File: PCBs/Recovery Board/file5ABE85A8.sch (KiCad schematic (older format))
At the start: 3 parts

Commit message: review changes + instr board PCB
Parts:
- gave numbers to parts that had none: 3
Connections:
- net VccA: now also U2.5 (EN)
- net VccB: no longer U2.5 (EN)
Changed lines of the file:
@@
 $EndDescr
 $Comp
-L PI4ULS5V201TAEX U?
+L PI4ULS5V201TAEX U2
 U 1 1 5ABE85EB
 P 5400 3750
-F 0 "U?" H 5400 4300 60  0000 C CNN
+AR Path="/5ABE85A9/5ABE85EB" Ref="U2"  Part="1"
+AR Path="/5ABEAE41/5ABE85EB" Ref="U3"  Part="1"
+F 0 "U3" H 5400 4300 60  0000 C CNN
 F 1 "PI4ULS5V201TAEX" H 5400 3650 60  0000 C CNN
 F 2 "" H 5400 3750 60  0001 C CNN
@@
 $EndComp
 $Comp
-L C C?
+L C C6
 U 1 1 5ABE8664
 P 6250 3950
-F 0 "C?" H 6275 4050 50  0000 L CNN
+AR Path="/5ABE85A9/5ABE8664" Ref="C6"  Part="1"
+AR Path="/5ABEAE41/5ABE8664" Ref="C8"  Part="1"
+F 0 "C8" H 6275 4050 50  0000 L CNN
 F 1 "0.1uF" H 6275 3850 50  0000 L CNN
 F 2 "" H 6288 3800 50  0001 C CNN
@@
 $EndComp
 $Comp
-L C C?
+L C C5
 U 1 1 5ABE8691
 P 4550 3800
-F 0 "C?" H 4575 3900 50  0000 L CNN
+AR Path="/5ABE85A9/5ABE8691" Ref="C5"  Part="1"
+AR Path="/5ABEAE41/5ABE8691" Ref="C7"  Part="1"
+F 0 "C7" H 4575 3900 50  0000 L CNN
 F 1 "0.1uF" H 4575 3700 50  0000 L CNN
 F 2 "" H 4588 3650 50  0001 C CNN
@@
 	4550 3400 4950 3400
 $Comp
-L GND #PWR?
+L GND #PWR16
 U 1 1 5ABE86F6
 P 4550 3950
-F 0 "#PWR?" H 4550 3700 50  0001 C CNN
+AR Path="/5ABE85A9/5ABE86F6" Ref="#PWR16"  Part="1"
+AR Path="/5ABEAE41/5ABE86F6" Ref="#PWR19"  Part="1"
+F 0 "#PWR19" H 4550 3700 50  0001 C CNN
 F 1 "GND" H 4550 3800 50  0000 C CNN
 F 2 "" H 4550 3950 50  0001 C CNN
@@
 $EndComp
 $Comp
-L GND #PWR?
+L GND #PWR17
 U 1 1 5ABE8711
 P 4850 3950
-F 0 "#PWR?" H 4850 3700 50  0001 C CNN
+AR Path="/5ABE85A9/5ABE8711" Ref="#PWR17"  Part="1"
+AR Path="/5ABEAE41/5ABE8711" Ref="#PWR20"  Part="1"
+F 0 "#PWR20" H 4850 3700 50  0001 C CNN
 F 1 "GND" H 4850 3800 50  0000 C CNN
 F 2 "" H 4850 3950 50  0001 C CNN
@@
 $EndComp
 $Comp
-L GND #PWR?
+L GND #PWR18
 U 1 1 5ABE8725
 P 6250 4100
-F 0 "#PWR?" H 6250 3850 50  0001 C CNN
+AR Path="/5ABE85A9/5ABE8725" Ref="#PWR18"  Part="1"
+AR Path="/5ABEAE41/5ABE8725" Ref="#PWR21"  Part="1"
+F 0 "#PWR21" H 6250 3850 50  0001 C CNN
 F 1 "GND" H 6250 3950 50  0000 C CNN
 F 2 "" H 6250 4100 50  0001 C CNN
@@
 Wire Wire Line
 	6250 3400 6250 3800
-Wire Wire Line
-	5850 3700 6250 3700
-Connection ~ 6250 3700
 Wire Wire Line
 	4950 3700 4850 3700
@@
 Text HLabel 5850 3600 2    60   Input ~ 0
 B
+Wire Wire Line
+	5850 3700 5850 4200
+Wire Wire Line
+	5850 4200 4300 4200
+Wire Wire Line
+	4300 4200 4300 3550
+Wire Wire Line
+	4300 3550 4550 3550
+Connection ~ 4550 3550
 $EndSCHEMATC

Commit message: Updated Recovery Netlist, started board updated layout
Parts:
- U2: footprint (none) -> sot:SOT-23-6
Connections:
- net A: no longer U2.2 (A)
- net B: no longer U2.6 (B)
- no-connect marks 2 -> 0
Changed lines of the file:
@@
 LIBS:fgpmmopa6h
 LIBS:sot-223
-LIBS:Placeholders
 LIBS:Recovery Board Parts
 LIBS:ap2204k-5
@@
 Comment4 ""
 $EndDescr
-$Comp
-L PI4ULS5V201TAEX U2
-U 1 1 5ABE85EB
-P 5400 3750
-AR Path="/5ABE85A9/5ABE85EB" Ref="U2"  Part="1"
-AR Path="/5ABEAE41/5ABE85EB" Ref="U3"  Part="1"
-F 0 "U3" H 5400 4300 60  0000 C CNN
-F 1 "PI4ULS5V201TAEX" H 5400 3650 60  0000 C CNN
-F 2 "" H 5400 3750 60  0001 C CNN
-F 3 "" H 5400 3750 60  0001 C CNN
-	1    5400 3750
-	1    0    0    -1
-$EndComp
 $Comp
 L C C6
@@
 	4550 3400 4950 3400
 $Comp
-L GND #PWR16
+L GND #PWR016
 U 1 1 5ABE86F6
 P 4550 3950
-AR Path="/5ABE85A9/5ABE86F6" Ref="#PWR16"  Part="1"
-AR Path="/5ABEAE41/5ABE86F6" Ref="#PWR19"  Part="1"
-F 0 "#PWR19" H 4550 3700 50  0001 C CNN
+AR Path="/5ABE85A9/5ABE86F6" Ref="#PWR016"  Part="1"
+AR Path="/5ABEAE41/5ABE86F6" Ref="#PWR019"  Part="1"
+F 0 "#PWR019" H 4550 3700 50  0001 C CNN
 F 1 "GND" H 4550 3800 50  0000 C CNN
 F 2 "" H 4550 3950 50  0001 C CNN
@@
 $EndComp
 $Comp
-L GND #PWR17
+L GND #PWR017
 U 1 1 5ABE8711
 P 4850 3950
-AR Path="/5ABE85A9/5ABE8711" Ref="#PWR17"  Part="1"
-AR Path="/5ABEAE41/5ABE8711" Ref="#PWR20"  Part="1"
-F 0 "#PWR20" H 4850 3700 50  0001 C CNN
+AR Path="/5ABE85A9/5ABE8711" Ref="#PWR017"  Part="1"
+AR Path="/5ABEAE41/5ABE8711" Ref="#PWR020"  Part="1"
+F 0 "#PWR020" H 4850 3700 50  0001 C CNN
 F 1 "GND" H 4850 3800 50  0000 C CNN
 F 2 "" H 4850 3950 50  0001 C CNN
@@
 $EndComp
 $Comp
-L GND #PWR18
+L GND #PWR018
 U 1 1 5ABE8725
 P 6250 4100
-AR Path="/5ABE85A9/5ABE8725" Ref="#PWR18"  Part="1"
-AR Path="/5ABEAE41/5ABE8725" Ref="#PWR21"  Part="1"
-F 0 "#PWR21" H 6250 3850 50  0001 C CNN
+AR Path="/5ABE85A9/5ABE8725" Ref="#PWR018"  Part="1"
+AR Path="/5ABEAE41/5ABE8725" Ref="#PWR021"  Part="1"
+F 0 "#PWR021" H 6250 3850 50  0001 C CNN
 F 1 "GND" H 6250 3950 50  0000 C CNN
 F 2 "" H 6250 4100 50  0001 C CNN
@@
 Wire Wire Line
 	4850 3700 4850 3950
-NoConn ~ 5850 3500
-NoConn ~ 4950 3600
-Text HLabel 4950 3500 0    60   Input ~ 0
+Text HLabel 4950 3550 0    60   Input ~ 0
 A
 Text HLabel 4550 3400 0    60   Input ~ 0
@@
 Text HLabel 6250 3400 2    60   Input ~ 0
 VccB
-Text HLabel 5850 3600 2    60   Input ~ 0
+Text HLabel 5850 3550 2    60   Input ~ 0
 B
 Wire Wire Line
@@
 	4300 3550 4550 3550
 Connection ~ 4550 3550
+$Comp
+L PI4ULS5V201TAEX U2
+U 1 1 5ABE85EB
+P 5400 3750
+AR Path="/5ABE85A9/5ABE85EB" Ref="U2"  Part="1"
+AR Path="/5ABEAE41/5ABE85EB" Ref="U3"  Part="1"
+F 0 "U3" H 5400 4300 60  0000 C CNN
+F 1 "PI4ULS5V201TAEX" H 5400 3650 60  0000 C CNN
+F 2 "sot:SOT-23-6" H 5400 3750 60  0001 C CNN
+F 3 "" H 5400 3750 60  0001 C CNN
+	1    5400 3750
+	1    0    0    -1
+$EndComp
 $EndSCHEMATC

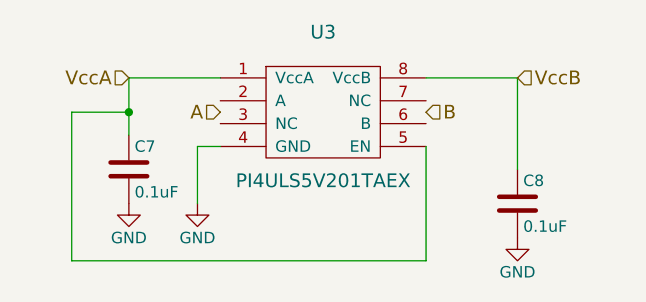
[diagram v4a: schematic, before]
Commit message: Finished updating recovery board layout
board layout, schematic and netlist up to date
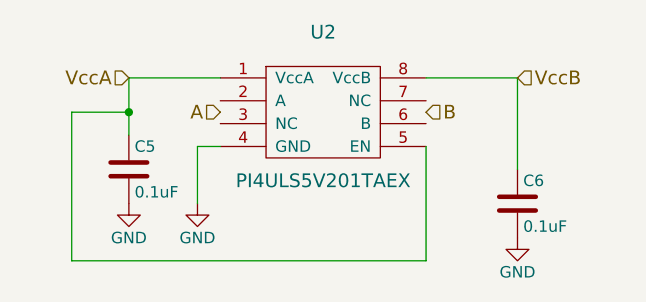
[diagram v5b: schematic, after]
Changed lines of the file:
@@
 $Descr A4 11693 8268
 encoding utf-8
-Sheet 3 3
+Sheet 2 3
 Title ""
 Date ""
@@
 AR Path="/5ABE85A9/5ABE8664" Ref="C6"  Part="1"
 AR Path="/5ABEAE41/5ABE8664" Ref="C8"  Part="1"
-F 0 "C8" H 6275 4050 50  0000 L CNN
+F 0 "C6" H 6275 4050 50  0000 L CNN
 F 1 "0.1uF" H 6275 3850 50  0000 L CNN
 F 2 "" H 6288 3800 50  0001 C CNN
@@
 AR Path="/5ABE85A9/5ABE8691" Ref="C5"  Part="1"
 AR Path="/5ABEAE41/5ABE8691" Ref="C7"  Part="1"
-F 0 "C7" H 4575 3900 50  0000 L CNN
+F 0 "C5" H 4575 3900 50  0000 L CNN
 F 1 "0.1uF" H 4575 3700 50  0000 L CNN
 F 2 "" H 4588 3650 50  0001 C CNN
@@
 AR Path="/5ABE85A9/5ABE86F6" Ref="#PWR016"  Part="1"
 AR Path="/5ABEAE41/5ABE86F6" Ref="#PWR019"  Part="1"
-F 0 "#PWR019" H 4550 3700 50  0001 C CNN
+F 0 "#PWR016" H 4550 3700 50  0001 C CNN
 F 1 "GND" H 4550 3800 50  0000 C CNN
 F 2 "" H 4550 3950 50  0001 C CNN
@@
 AR Path="/5ABE85A9/5ABE8711" Ref="#PWR017"  Part="1"
 AR Path="/5ABEAE41/5ABE8711" Ref="#PWR020"  Part="1"
-F 0 "#PWR020" H 4850 3700 50  0001 C CNN
+F 0 "#PWR017" H 4850 3700 50  0001 C CNN
 F 1 "GND" H 4850 3800 50  0000 C CNN
 F 2 "" H 4850 3950 50  0001 C CNN
@@
 AR Path="/5ABE85A9/5ABE8725" Ref="#PWR018"  Part="1"
 AR Path="/5ABEAE41/5ABE8725" Ref="#PWR021"  Part="1"
-F 0 "#PWR021" H 6250 3850 50  0001 C CNN
+F 0 "#PWR018" H 6250 3850 50  0001 C CNN
 F 1 "GND" H 6250 3950 50  0000 C CNN
 F 2 "" H 6250 4100 50  0001 C CNN
@@
 AR Path="/5ABE85A9/5ABE85EB" Ref="U2"  Part="1"
 AR Path="/5ABEAE41/5ABE85EB" Ref="U3"  Part="1"
-F 0 "U3" H 5400 4300 60  0000 C CNN
+F 0 "U2" H 5400 4300 60  0000 C CNN
 F 1 "PI4ULS5V201TAEX" H 5400 3650 60  0000 C CNN
 F 2 "sot:SOT-23-6" H 5400 3750 60  0001 C CNN

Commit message: swapped all mounting holes with plated ones, fixed disconnected components on recovery, added the 4 decoupling caps to recovery, fixed silk screen on pads in instr, fixed traces connecting through pads on recovery and instr, moved q1 on instr, brought trace in near u2 on instr, switched u2 & u3 to hand solder on instr, fixed xbee screen on recovery, fixed connector labels on recovery, removed recovery dims past edge cuts, fixed pad mask clearance on recovery
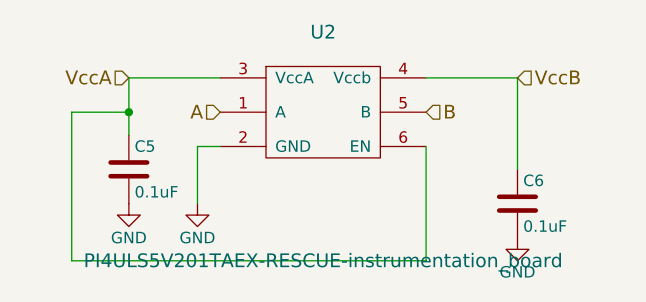
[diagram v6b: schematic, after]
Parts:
- removed U2: PI4ULS5V201TAEX, sot:SOT-23-6, symbol PI4ULS5V201TAEX
- added U2: PI4ULS5V201TAEX-RESCUE-instrumentation_board, TO_SOT_Packages_SMD:SOT-23-6_Handsoldering, symbol PI4ULS5V201TAEX-RESCUE-instrumentation_board
- C5, C6: footprint (none) -> Capacitors_SMD:C_0805_HandSoldering
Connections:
- net A: now also U2.1 (A)
- net B: now also U2.5 (B)
- net GND: now also U2.2 (GND)
- net VccA: now also U2.3 (VccA), U2.6 (EN)
- net VccB: now also U2.4 (Vccb)
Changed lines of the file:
@@
 LIBS:fgpmmopa6h
 LIBS:sot-223
+LIBS:Placeholders
 LIBS:Recovery Board Parts
 LIBS:ap2204k-5
 LIBS:Recovery Board-cache
 LIBS:instrumentation_board_parts
+LIBS:instrumentation_board-cache
 EELAYER 25 0
 EELAYER END
@@
 F 0 "C6" H 6275 4050 50  0000 L CNN
 F 1 "0.1uF" H 6275 3850 50  0000 L CNN
-F 2 "" H 6288 3800 50  0001 C CNN
+F 2 "Capacitors_SMD:C_0805_HandSoldering" H 6288 3800 50  0001 C CNN
 F 3 "" H 6250 3950 50  0001 C CNN
 	1    6250 3950
@@
 F 0 "C5" H 4575 3900 50  0000 L CNN
 F 1 "0.1uF" H 4575 3700 50  0000 L CNN
-F 2 "" H 4588 3650 50  0001 C CNN
+F 2 "Capacitors_SMD:C_0805_HandSoldering" H 4588 3650 50  0001 C CNN
 F 3 "" H 4550 3800 50  0001 C CNN
 	1    4550 3800
@@
 AR Path="/5ABE85A9/5ABE86F6" Ref="#PWR016"  Part="1"
 AR Path="/5ABEAE41/5ABE86F6" Ref="#PWR019"  Part="1"
-F 0 "#PWR016" H 4550 3700 50  0001 C CNN
+F 0 "#PWR019" H 4550 3700 50  0001 C CNN
 F 1 "GND" H 4550 3800 50  0000 C CNN
 F 2 "" H 4550 3950 50  0001 C CNN
@@
 AR Path="/5ABE85A9/5ABE8711" Ref="#PWR017"  Part="1"
 AR Path="/5ABEAE41/5ABE8711" Ref="#PWR020"  Part="1"
-F 0 "#PWR017" H 4850 3700 50  0001 C CNN
+F 0 "#PWR020" H 4850 3700 50  0001 C CNN
 F 1 "GND" H 4850 3800 50  0000 C CNN
 F 2 "" H 4850 3950 50  0001 C CNN
@@
 AR Path="/5ABE85A9/5ABE8725" Ref="#PWR018"  Part="1"
 AR Path="/5ABEAE41/5ABE8725" Ref="#PWR021"  Part="1"
-F 0 "#PWR018" H 6250 3850 50  0001 C CNN
+F 0 "#PWR021" H 6250 3850 50  0001 C CNN
 F 1 "GND" H 6250 3950 50  0000 C CNN
 F 2 "" H 6250 4100 50  0001 C CNN
@@
 Connection ~ 4550 3550
 $Comp
-L PI4ULS5V201TAEX U2
-U 1 1 5ABE85EB
+L PI4ULS5V201TAEX-RESCUE-instrumentation_board U2
+U 1 1 5AC6DC41
 P 5400 3750
-AR Path="/5ABE85A9/5ABE85EB" Ref="U2"  Part="1"
-AR Path="/5ABEAE41/5ABE85EB" Ref="U3"  Part="1"
+AR Path="/5ABE85A9/5AC6DC41" Ref="U2"  Part="1"
+AR Path="/5ABEAE41/5AC6DC41" Ref="U3"  Part="1"
 F 0 "U2" H 5400 4300 60  0000 C CNN
-F 1 "PI4ULS5V201TAEX" H 5400 3650 60  0000 C CNN
-F 2 "sot:SOT-23-6" H 5400 3750 60  0001 C CNN
+F 1 "PI4ULS5V201TAEX-RESCUE-instrumentation_board" H 5400 3300 60  0000 C CNN
+F 2 "TO_SOT_Packages_SMD:SOT-23-6_Handsoldering" H 5400 3750 60  0001 C CNN
 F 3 "" H 5400 3750 60  0001 C CNN
 	1    5400 3750

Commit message: Changed connectors for recovery board batteries
Added a second connector for the other battery
Moved connectors to top of board
Replaced footprint with JST-PH
Extended board width
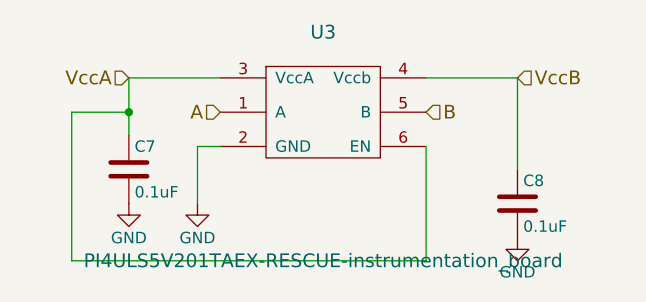
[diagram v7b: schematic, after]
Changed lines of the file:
@@
 AR Path="/5ABE85A9/5ABE8664" Ref="C6"  Part="1"
 AR Path="/5ABEAE41/5ABE8664" Ref="C8"  Part="1"
-F 0 "C6" H 6275 4050 50  0000 L CNN
+F 0 "C8" H 6275 4050 50  0000 L CNN
 F 1 "0.1uF" H 6275 3850 50  0000 L CNN
 F 2 "Capacitors_SMD:C_0805_HandSoldering" H 6288 3800 50  0001 C CNN
@@
 AR Path="/5ABE85A9/5ABE8691" Ref="C5"  Part="1"
 AR Path="/5ABEAE41/5ABE8691" Ref="C7"  Part="1"
-F 0 "C5" H 4575 3900 50  0000 L CNN
+F 0 "C7" H 4575 3900 50  0000 L CNN
 F 1 "0.1uF" H 4575 3700 50  0000 L CNN
 F 2 "Capacitors_SMD:C_0805_HandSoldering" H 4588 3650 50  0001 C CNN
@@
 AR Path="/5ABE85A9/5AC6DC41" Ref="U2"  Part="1"
 AR Path="/5ABEAE41/5AC6DC41" Ref="U3"  Part="1"
-F 0 "U2" H 5400 4300 60  0000 C CNN
+F 0 "U3" H 5400 4300 60  0000 C CNN
 F 1 "PI4ULS5V201TAEX-RESCUE-instrumentation_board" H 5400 3300 60  0000 C CNN
 F 2 "TO_SOT_Packages_SMD:SOT-23-6_Handsoldering" H 5400 3750 60  0001 C CNN
